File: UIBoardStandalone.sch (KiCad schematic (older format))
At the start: 46 parts, among them J10 Conn_02x15_Odd_Even, J14 Conn_02x01, J17 Conn_02x08_Odd_Even, SW1 Button_P, SW10 Button_4, SW11 Button_8, SW12 Button_0, SW13 Button_2, SW14 Button_5, SW15 Button_3, SW16 Button_6, SW17 Button_9, SW18 Button_Z, SW2 Button_X, SW3 Button_S, SW4 Button_G, SW5 Button_R, SW6 Button_M, SW7 Button_7, SW8 Button_Y, SW9 Button_1, U10 MM74C923

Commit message: [modified:] Datasheet cleanup [modified:] lib cleanup [fix:] removed voltmeter from uiboard [fix:] mic audio jack terminal mix-up
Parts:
- removed J14: Conn_02x01, symbol Connector_Generic:Conn_02x01
- removed MES1: Voltmeter_DC, symbol Device:Voltmeter_DC
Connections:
- net labels removed: Signal_Strngth_Dial_+, Signal_Strngth_Dial_-
- wire segments 480 -> 476
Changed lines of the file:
@@
 	3950 7600 3950 7850
-$Comp
-L Device:Voltmeter_DC MES1
-U 1 1 5FEEEACA
-P 9450 4600
-F 0 "MES1" H 9603 4646 50  0000 L CNN
-F 1 "Voltmeter_DC" H 9603 4555 50  0000 L CNN
-F 2 "" V 9450 4700 50  0001 C CNN
-F 3 "~" V 9450 4700 50  0001 C CNN
-	1    9450 4600
-	1    0    0    -1
-$EndComp
 $Comp
 L Connector_Generic:Conn_02x15_Odd_Even J?
@@
 Text Label 3050 5250 0    50   ~ 0
 Pinline_VCC
-$Comp
-L Connector_Generic:Conn_02x01 J?
-U 1 1 6A6FC93C
-P 9450 5300
-AR Path="/6A6FC93C" Ref="J?"  Part="1"
-AR Path="/6101166B/6A6FC93C" Ref="J14"  Part="1"
-F 0 "J14" H 9500 5517 50  0000 C CNN
-F 1 "Conn_02x01" H 9500 5426 50  0000 C CNN
-F 2 "" H 9450 5300 50  0001 C CNN
-F 3 "~" H 9450 5300 50  0001 C CNN
-	1    9450 5300
-	1    0    0    -1
-$EndComp
-Text HLabel 9750 5300 2    50   UnSpc ~ 0
-Signal_Strngth_Dial_+
-Text HLabel 9250 5300 0    50   UnSpc ~ 0
-Signal_Strngth_Dial_-
-Wire Wire Line
-	9750 5300 9750 4400
-Wire Wire Line
-	9750 4400 9450 4400
-Wire Wire Line
-	9450 4800 9250 4800
-Wire Wire Line
-	9250 4800 9250 5300
 Wire Wire Line
 	2750 3850 3050 3850

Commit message: Alle Libs zusammengefasst in TeKaDe.lib Power Supply mit Standartbauteilen (nicht das Import Zeugs)
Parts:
- U? (x16): symbol hd1077r:HD1077R -> TeKaDe:HD1077R
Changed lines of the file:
@@
 	13300 4100 13500 4100
 $Comp
-L hd1077r:HD1077R U?
+L TeKaDe:HD1077R U?
 U 1 1 61846D93
 P 3300 800
@@
 $EndComp
 $Comp
-L hd1077r:HD1077R U?
+L TeKaDe:HD1077R U?
 U 1 1 618635E6
 P 4050 800
@@
 $EndComp
 $Comp
-L hd1077r:HD1077R U?
+L TeKaDe:HD1077R U?
 U 1 1 6187EE3E
 P 4750 800
@@
 $EndComp
 $Comp
-L hd1077r:HD1077R U?
+L TeKaDe:HD1077R U?
 U 1 1 6187EE44
 P 5500 800
@@
 $EndComp
 $Comp
-L hd1077r:HD1077R U?
+L TeKaDe:HD1077R U?
 U 1 1 6189C8E7
 P 6950 800
@@
 $EndComp
 $Comp
-L hd1077r:HD1077R U?
+L TeKaDe:HD1077R U?
 U 1 1 6189C8ED
 P 7650 800
@@
 $EndComp
 $Comp
-L hd1077r:HD1077R U?
+L TeKaDe:HD1077R U?
 U 1 1 6189C8F3
 P 8400 800
@@
 $EndComp
 $Comp
-L hd1077r:HD1077R U?
+L TeKaDe:HD1077R U?
 U 1 1 618B84C4
 P 9050 800
@@
 $EndComp
 $Comp
-L hd1077r:HD1077R U?
+L TeKaDe:HD1077R U?
 U 1 1 618B84CA
 P 9800 800
@@
 $EndComp
 $Comp
-L hd1077r:HD1077R U?
+L TeKaDe:HD1077R U?
 U 1 1 618B84D0
 P 10500 800
@@
 $EndComp
 $Comp
-L hd1077r:HD1077R U?
+L TeKaDe:HD1077R U?
 U 1 1 618B84D6
 P 11250 800
@@
 $EndComp
 $Comp
-L hd1077r:HD1077R U?
+L TeKaDe:HD1077R U?
 U 1 1 618D410F
 P 12000 800
@@
 $EndComp
 $Comp
-L hd1077r:HD1077R U?
+L TeKaDe:HD1077R U?
 U 1 1 618D4115
 P 12750 800
@@
 $EndComp
 $Comp
-L hd1077r:HD1077R U?
+L TeKaDe:HD1077R U?
 U 1 1 618D411B
 P 13450 800
@@
 $EndComp
 $Comp
-L hd1077r:HD1077R U?
+L TeKaDe:HD1077R U?
 U 1 1 618D4121
 P 14200 800
@@
 	10950 2000 11700 2000
 $Comp
-L hd1077r:HD1077R U?
+L TeKaDe:HD1077R U?
 U 1 1 6189C8E1
 P 6200 800

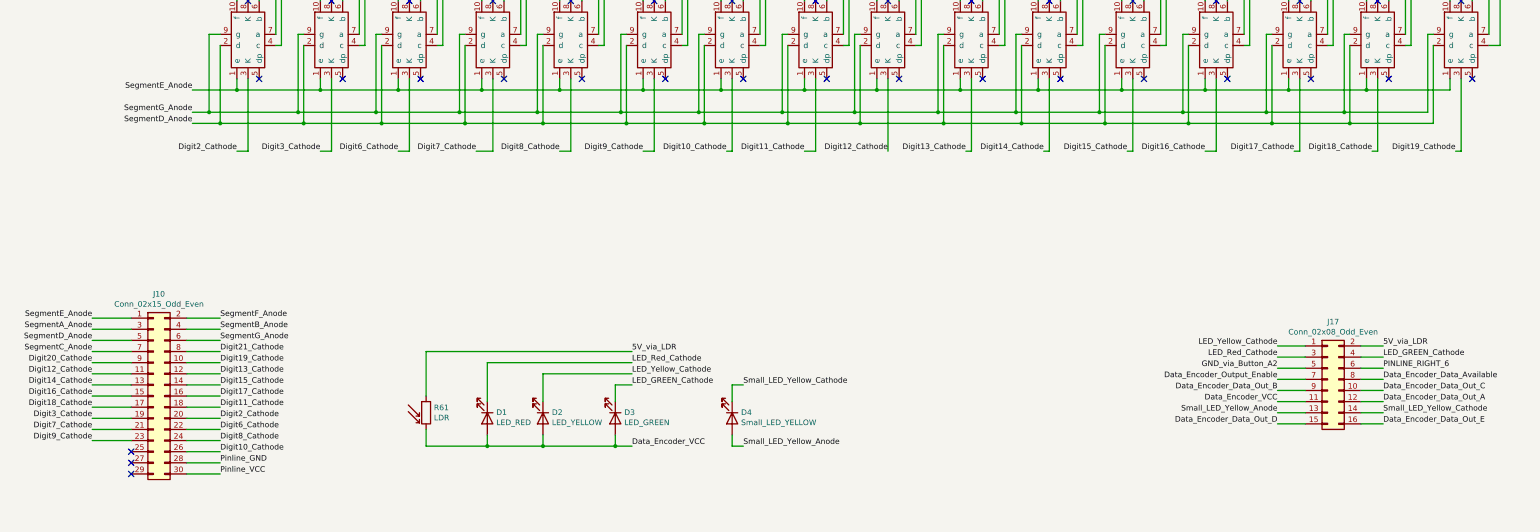
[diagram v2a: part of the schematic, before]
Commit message: [modified:] Digit nomenclature clarification
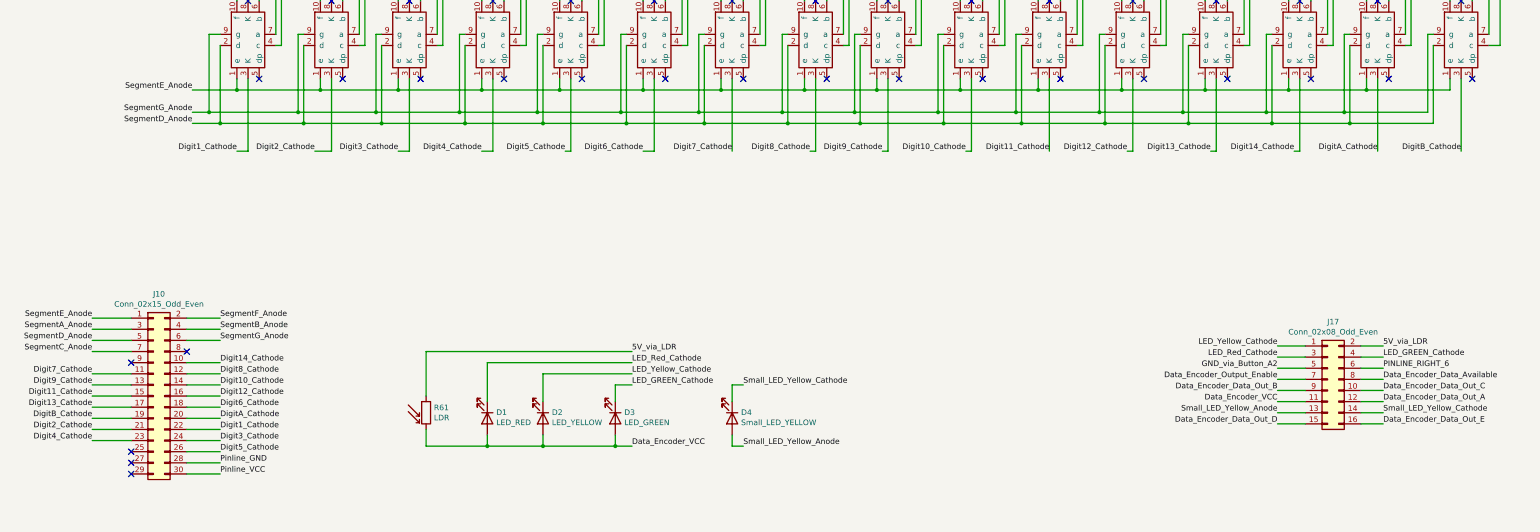
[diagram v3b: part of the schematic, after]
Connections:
- net Digit10_Cathode: now also J10.14 (Pin_14), U?.3 (K); no longer J10.26 (Pin_26), U?.3 (K)
- net Digit11_Cathode: now also J10.15 (Pin_15), U?.3 (K); no longer J10.18 (Pin_18), U?.3 (K)
- net Digit12_Cathode: now also J10.16 (Pin_16), U?.3 (K); no longer J10.11 (Pin_11), U?.3 (K)
- net Digit13_Cathode: now also J10.17 (Pin_17), U?.3 (K); no longer J10.12 (Pin_12), U?.3 (K)
- net Digit14_Cathode: now also J10.10 (Pin_10), U?.3 (K); no longer J10.13 (Pin_13), U?.3 (K)
- net Digit2_Cathode: now also J10.21 (Pin_21), U?.3 (K); no longer J10.20 (Pin_20), U?.3 (K)
- net Digit3_Cathode: now also J10.24 (Pin_24), U?.3 (K); no longer J10.19 (Pin_19), U?.3 (K)
- net Digit6_Cathode: now also J10.18 (Pin_18), U?.3 (K); no longer J10.22 (Pin_22), U?.3 (K)
- net Digit7_Cathode: now also J10.11 (Pin_11), U?.3 (K); no longer J10.21 (Pin_21), U?.3 (K)
- net Digit8_Cathode: now also J10.12 (Pin_12), U?.3 (K); no longer J10.24 (Pin_24), U?.3 (K)
- net Digit9_Cathode: now also J10.13 (Pin_13), U?.3 (K); no longer J10.23 (Pin_23), U?.3 (K)
- removed net Digit15_Cathode: J10.14 (Pin_14), U?.3 (K)
- removed net Digit16_Cathode: J10.15 (Pin_15), U?.3 (K)
- removed net Digit17_Cathode: J10.16 (Pin_16), U?.3 (K)
- net Digit18_Cathode renamed DigitA_Cathode
- net DigitA_Cathode: now also J10.20 (Pin_20); no longer J10.17 (Pin_17)
- net Digit19_Cathode renamed DigitB_Cathode
- net DigitB_Cathode: now also J10.19 (Pin_19); no longer J10.10 (Pin_10)
- net Digit20_Cathode: no longer names the net of J10.9 (Pin_9)
- net Digit21_Cathode: no longer names the net of J10.8 (Pin_8)
- new net Digit1_Cathode: J10.22 (Pin_22), U?.3 (K)
- new net Digit4_Cathode: J10.23 (Pin_23), U?.3 (K)
- new net Digit5_Cathode: J10.26 (Pin_26), U?.3 (K)
- no-connect marks 35 -> 37
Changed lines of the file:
@@
 $EndComp
 Text Label 1900 4950 2    50   ~ 0
+Digit4_Cathode
+Text Label 1900 4850 2    50   ~ 0
+Digit2_Cathode
+Text Label 1900 4750 2    50   ~ 0
+DigitB_Cathode
+Text Label 1900 4650 2    50   ~ 0
+Digit13_Cathode
+Text Label 1900 4550 2    50   ~ 0
+Digit11_Cathode
+Text Label 1900 4450 2    50   ~ 0
 Digit9_Cathode
-Text Label 1900 4850 2    50   ~ 0
+Text Label 1900 4350 2    50   ~ 0
 Digit7_Cathode
-Text Label 1900 4750 2    50   ~ 0
-Digit3_Cathode
-Text Label 1900 4650 2    50   ~ 0
-Digit18_Cathode
-Text Label 1900 4550 2    50   ~ 0
-Digit16_Cathode
-Text Label 1900 4450 2    50   ~ 0
-Digit14_Cathode
-Text Label 1900 4350 2    50   ~ 0
-Digit12_Cathode
-Text Label 1900 4250 2    50   ~ 0
-Digit20_Cathode
 Text Label 1900 4150 2    50   ~ 0
 SegmentC_Anode
@@
 Text Label 3050 4050 0    50   ~ 0
 SegmentG_Anode
-Text Label 3050 4150 0    50   ~ 0
-Digit21_Cathode
 Text Label 3050 4250 0    50   ~ 0
-Digit19_Cathode
+Digit14_Cathode
 Text Label 3050 4350 0    50   ~ 0
-Digit13_Cathode
+Digit8_Cathode
 Text Label 3050 4450 0    50   ~ 0
-Digit15_Cathode
+Digit10_Cathode
 Text Label 3050 4550 0    50   ~ 0
-Digit17_Cathode
+Digit12_Cathode
 Text Label 3050 4650 0    50   ~ 0
-Digit11_Cathode
+Digit6_Cathode
 Text Label 3050 4750 0    50   ~ 0
-Digit2_Cathode
+DigitA_Cathode
 Text Label 3050 4850 0    50   ~ 0
-Digit6_Cathode
+Digit1_Cathode
 Text Label 3050 4950 0    50   ~ 0
-Digit8_Cathode
+Digit3_Cathode
 Text Label 3050 5050 0    50   ~ 0
-Digit10_Cathode
+Digit5_Cathode
 Text Label 3050 5150 0    50   ~ 0
 Pinline_GND
@@
 	2750 4050 3050 4050
 Wire Wire Line
-	3050 4150 2750 4150
-Wire Wire Line
 	2750 4250 3050 4250
 Wire Wire Line
@@
 Wire Wire Line
 	2250 4350 1900 4350
-Wire Wire Line
-	1900 4250 2250 4250
 Wire Wire Line
 	2250 4150 1900 4150
@@
 Text Label 2800 2100 2    50   ~ 0
 SegmentD_Anode
+Text Label 13450 2350 2    50   ~ 0
+DigitA_Cathode
+Wire Wire Line
+	3300 2350 3200 2350
+Wire Wire Line
+	3300 1700 3300 2350
+Text Label 14200 2350 2    50   ~ 0
+DigitB_Cathode
+Text Label 12700 2350 2    50   ~ 0
+Digit14_Cathode
+Text Label 8350 2350 2    50   ~ 0
+Digit8_Cathode
+Text Label 9750 2350 2    50   ~ 0
+Digit10_Cathode
+Text Label 11200 2350 2    50   ~ 0
+Digit12_Cathode
+Text Label 6850 2350 2    50   ~ 0
+Digit6_Cathode
 Text Label 3200 2350 2    50   ~ 0
+Digit1_Cathode
+Text Label 4650 2350 2    50   ~ 0
+Digit3_Cathode
+Text Label 6150 2350 2    50   ~ 0
+Digit5_Cathode
+Text Label 5400 2350 2    50   ~ 0
+Digit4_Cathode
+Text Label 3900 2350 2    50   ~ 0
 Digit2_Cathode
-Wire Wire Line
-	3300 2350 3200 2350
-Wire Wire Line
-	3300 1700 3300 2350
-Text Label 3950 2350 2    50   ~ 0
-Digit3_Cathode
-Text Label 14150 2350 2    50   ~ 0
-Digit19_Cathode
-Text Label 9750 2350 2    50   ~ 0
+Text Label 11950 2350 2    50   ~ 0
 Digit13_Cathode
-Text Label 11200 2350 2    50   ~ 0
-Digit15_Cathode
-Text Label 12700 2350 2    50   ~ 0
-Digit17_Cathode
-Text Label 8300 2350 2    50   ~ 0
+Text Label 10500 2350 2    50   ~ 0
 Digit11_Cathode
-Text Label 4650 2350 2    50   ~ 0
-Digit6_Cathode
-Text Label 6100 2350 2    50   ~ 0
-Digit8_Cathode
-Text Label 7600 2350 2    50   ~ 0
-Digit10_Cathode
-Text Label 6850 2350 2    50   ~ 0
+Text Label 9000 2350 2    50   ~ 0
 Digit9_Cathode
-Text Label 5350 2350 2    50   ~ 0
+Text Label 7650 2350 2    50   ~ 0
 Digit7_Cathode
-Text Label 13400 2350 2    50   ~ 0
-Digit18_Cathode
-Text Label 11900 2350 2    50   ~ 0
-Digit16_Cathode
-Text Label 10450 2350 2    50   ~ 0
-Digit14_Cathode
-Text Label 9050 2350 2    50   ~ 0
-Digit12_Cathode
-Wire Wire Line
-	14150 2350 14200 2350
-Wire Wire Line
-	14200 1700 14200 2350
-Wire Wire Line
-	13450 2350 13400 2350
-Wire Wire Line
-	13450 1700 13450 2350
-Wire Wire Line
-	12750 2350 12700 2350
+Wire Wire Line
+	12700 2350 12750 2350
 Wire Wire Line
 	12750 1700 12750 2350
 Wire Wire Line
-	12000 2350 11900 2350
+	12000 2350 11950 2350
 Wire Wire Line
 	12000 1700 12000 2350
 Wire Wire Line
-	11200 2350 11250 2350
+	11250 2350 11200 2350
 Wire Wire Line
 	11250 1700 11250 2350
 Wire Wire Line
-	10500 2350 10450 2350
-Wire Wire Line
 	10500 1700 10500 2350
 Wire Wire Line
-	9800 2350 9750 2350
+	9750 2350 9800 2350
 Wire Wire Line
 	9800 1700 9800 2350
 Wire Wire Line
+	9050 2350 9000 2350
+Wire Wire Line
 	9050 1700 9050 2350
 Wire Wire Line
-	8400 2350 8300 2350
+	8400 2350 8350 2350
 Wire Wire Line
 	8400 1700 8400 2350
@@
 	7650 1700 7650 2350
 Wire Wire Line
-	6850 2350 6950 2350
+	6950 2350 6850 2350
 Wire Wire Line
 	6950 1700 6950 2350
@@
 	6200 1700 6200 2350
 Wire Wire Line
-	5500 2350 5350 2350
+	5400 2350 5500 2350
 Wire Wire Line
 	5500 1700 5500 2350
 Wire Wire Line
-	6100 2350 6200 2350
-Wire Wire Line
-	4750 2350 4650 2350
-Wire Wire Line
 	4750 1700 4750 2350
 Wire Wire Line
-	4050 2350 3950 2350
-Wire Wire Line
 	4050 1700 4050 2350
 Wire Wire Line
-	7600 2350 7650 2350
+	4650 2350 4750 2350
+Wire Wire Line
+	6150 2350 6200 2350
+Wire Wire Line
+	3900 2350 4050 2350
+Wire Wire Line
+	13450 2350 13450 1700
+Wire Wire Line
+	14200 2350 14200 1700
+NoConn ~ 2750 4150
+NoConn ~ 2250 4250
 $EndSCHEMATC

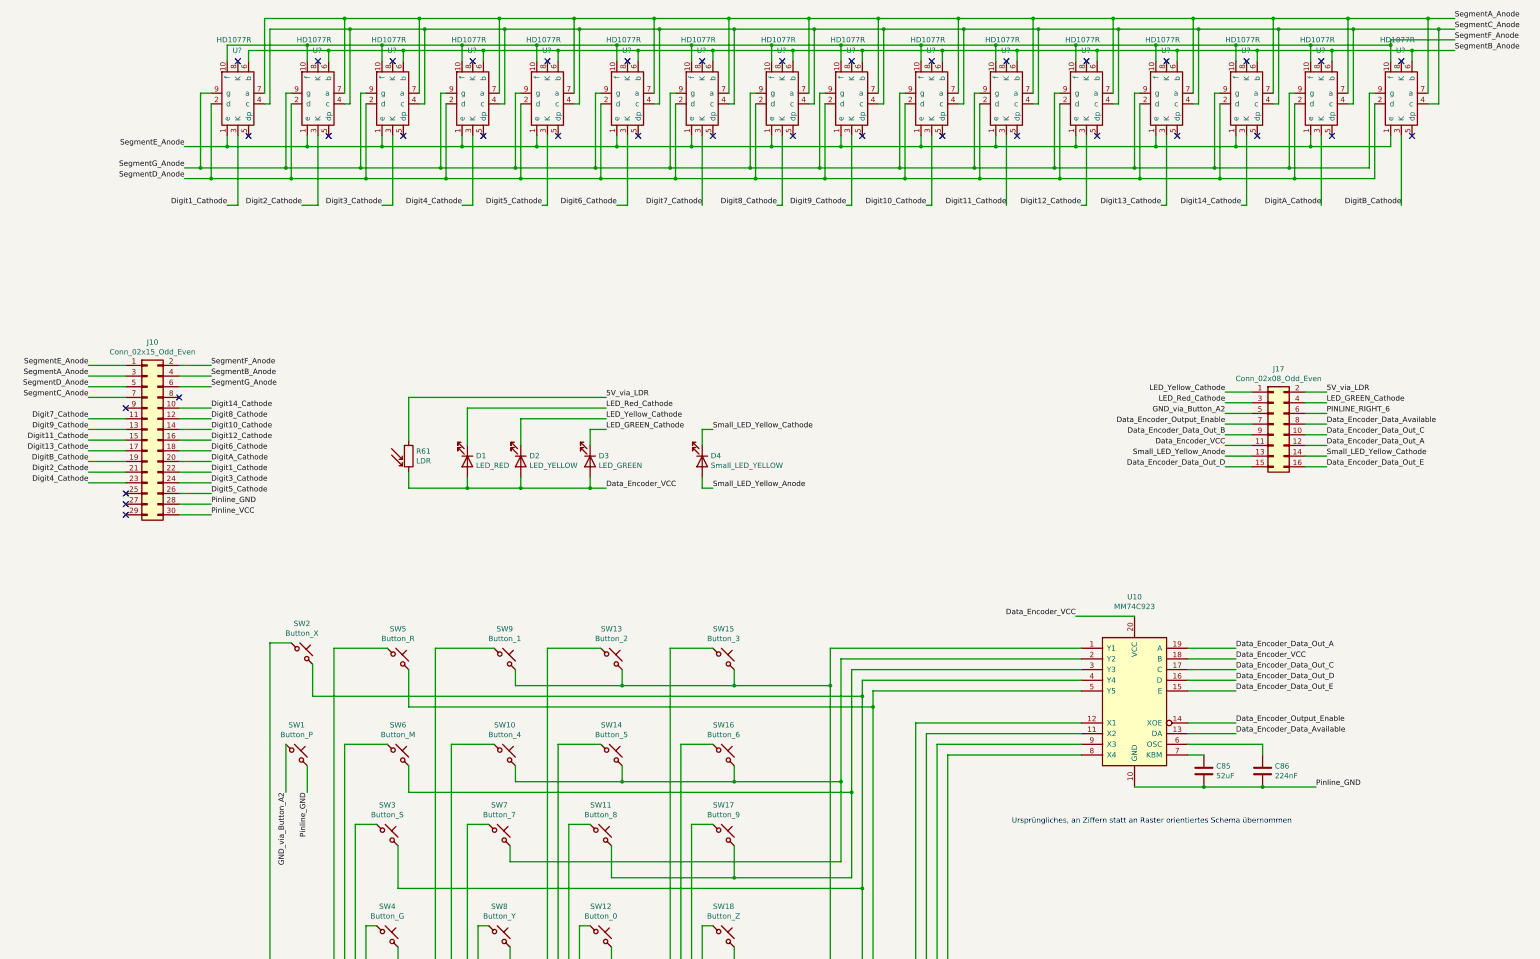
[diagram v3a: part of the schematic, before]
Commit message: [modified:] uln2003 package swap [modified:] Display nomenclature update
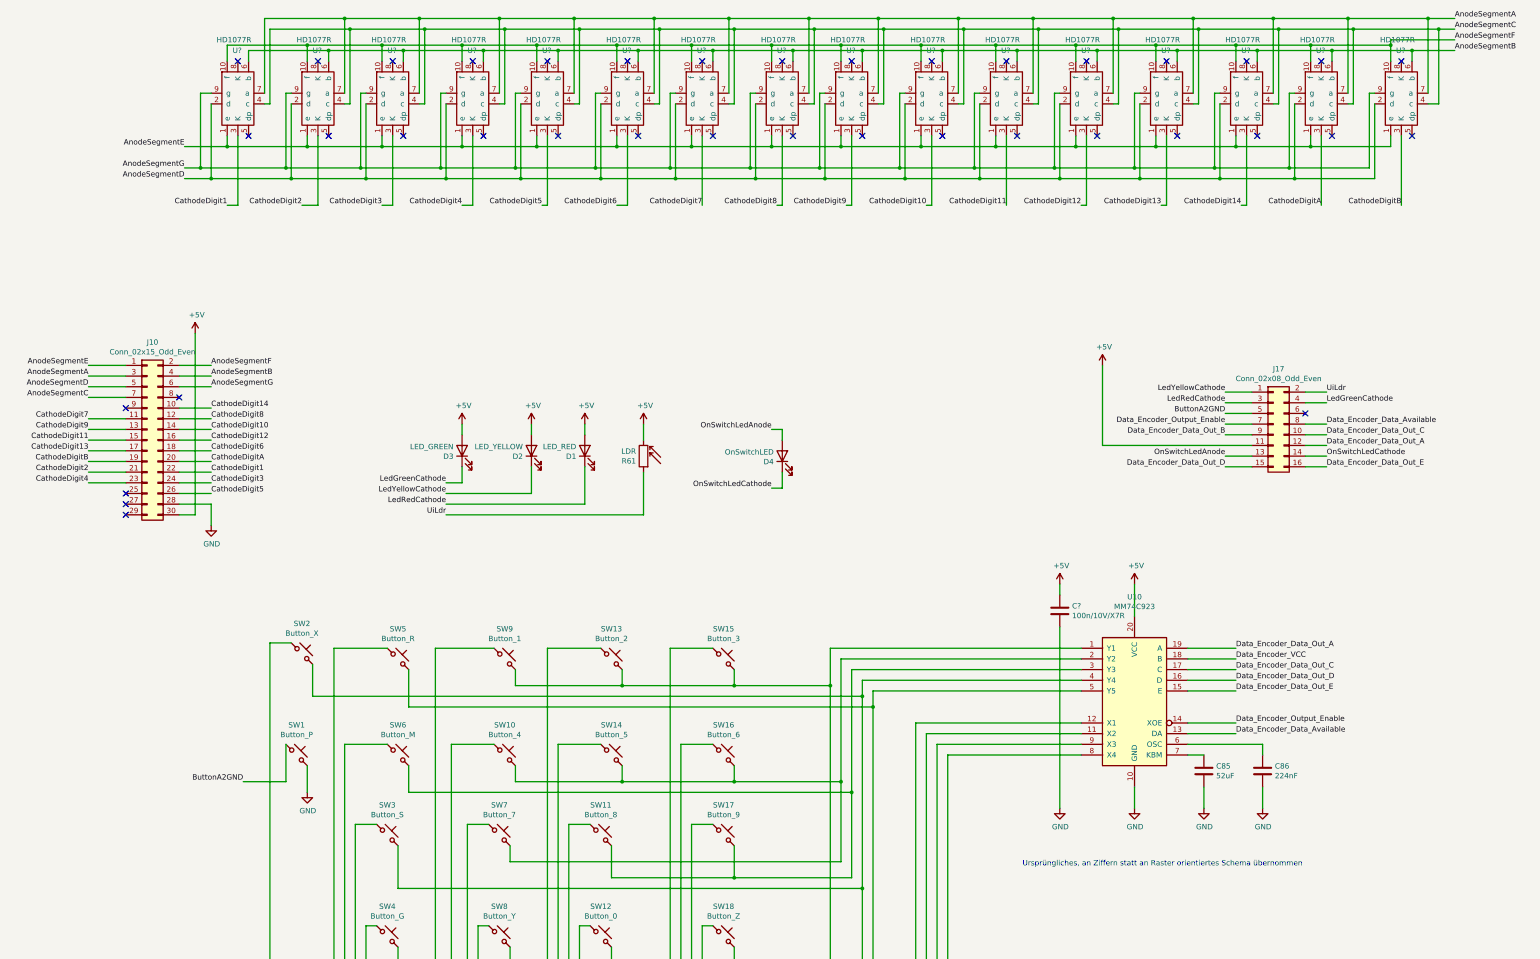
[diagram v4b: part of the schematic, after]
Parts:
- added C?: 100n/10V/X7R, Resistor_SMD:R_0603_1608Metric, symbol Device:C
- D4: value Small_LED_YELLOW -> OnSwitchLED
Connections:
- net Data_Encoder_VCC: no longer D1.2 (A), D2.2 (A), D3.2 (A), J17.11 (Pin_11), R61.2, U10.20 (VCC)
- net 5V_via_LDR renamed UiLdr
- net Digit10_Cathode renamed CathodeDigit10
- net Digit11_Cathode renamed CathodeDigit11
- net Digit12_Cathode renamed CathodeDigit12
- net Digit13_Cathode renamed CathodeDigit13
- net Digit14_Cathode renamed CathodeDigit14
- net Digit1_Cathode renamed CathodeDigit1
- net Digit2_Cathode renamed CathodeDigit2
- net Digit3_Cathode renamed CathodeDigit3
- net Digit4_Cathode renamed CathodeDigit4
- net Digit5_Cathode renamed CathodeDigit5
- net Digit6_Cathode renamed CathodeDigit6
- net Digit7_Cathode renamed CathodeDigit7
- net Digit8_Cathode renamed CathodeDigit8
- net Digit9_Cathode renamed CathodeDigit9
- net DigitA_Cathode renamed CathodeDigitA
- net DigitB_Cathode renamed CathodeDigitB
- net GND_via_Button_A2 renamed ButtonA2GND
- net LED_GREEN_Cathode renamed LedGreenCathode
- net LED_Red_Cathode renamed LedRedCathode
- net LED_Yellow_Cathode renamed LedYellowCathode
- net PINLINE_RIGHT_6: no longer names the net of J17.6 (Pin_6)
- net Pinline_GND renamed GND
- net GND: now also C?.2
- net Pinline_VCC renamed +5V
- net +5V: now also D1.2 (A), D2.2 (A), D3.2 (A), J17.11 (Pin_11), R61.2, U10.20 (VCC), C?.1
- net SegmentA_Anode renamed AnodeSegmentA
- net SegmentB_Anode renamed AnodeSegmentB
- net SegmentC_Anode renamed AnodeSegmentC
- net SegmentD_Anode renamed AnodeSegmentD
- net SegmentE_Anode renamed AnodeSegmentE
- net SegmentF_Anode renamed AnodeSegmentF
- net SegmentG_Anode renamed AnodeSegmentG
- net Small_LED_Yellow_Anode renamed OnSwitchLedAnode
- net Small_LED_Yellow_Cathode renamed OnSwitchLedCathode
- no-connect marks 37 -> 38
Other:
- moved on the sheet: D1, D2, D3, D4, R61

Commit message: - Platzoptimierungen
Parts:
- D4: value OnSwitchLED -> LED_ON
- J10: footprint (none) -> Connector_PinHeader_2.54mm:PinHeader_2x15_P2.54mm_Vertical
- J17: footprint (none) -> Connector_PinHeader_2.54mm:PinHeader_2x08_P2.54mm_Vertical
- U10: footprint (none) -> Package_SO:SOIC-20W_7.5x12.8mm_P1.27mm
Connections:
- net OnSwitchLedAnode is gone; now on net +5V: D4.2 (A), J17.13 (Pin_13)
- net LedGreenCathode renamed LED_GN
- net LedRedCathode renamed LED_RD
- net LedYellowCathode renamed LED_YL
- net OnSwitchLedCathode renamed LED_ON
- net UiLdr renamed LDR
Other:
- note added: "SignalStrength / Keyswitch connectoren?\n\nÄnderungen:\n- OnSwitchLedAnode durch 5V ersetzt\n- Footprint Konnektoren MALE"
- moved on the sheet: C?, D4, R61

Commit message: [fix:] general troublespots -> notes
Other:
- note added: "https://www.aeri.com/products/search/?q=hd1077\n"
- note added: "https://www.aeri.com/products/search/?q=mm74c923\n"
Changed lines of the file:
@@
 	1    0    0    -1
 $EndComp
+Text Notes 12100 6100 0    50   ~ 0
+https://www.aeri.com/products/search/?q=mm74c923\n
+Text Notes 15150 1400 0    50   ~ 0
+https://www.aeri.com/products/search/?q=hd1077\n
 $EndSCHEMATC
